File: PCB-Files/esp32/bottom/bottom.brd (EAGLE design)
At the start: 31 x 50 mm, 19 parts, among them X2 ESP32_WROOM32_SKINNY

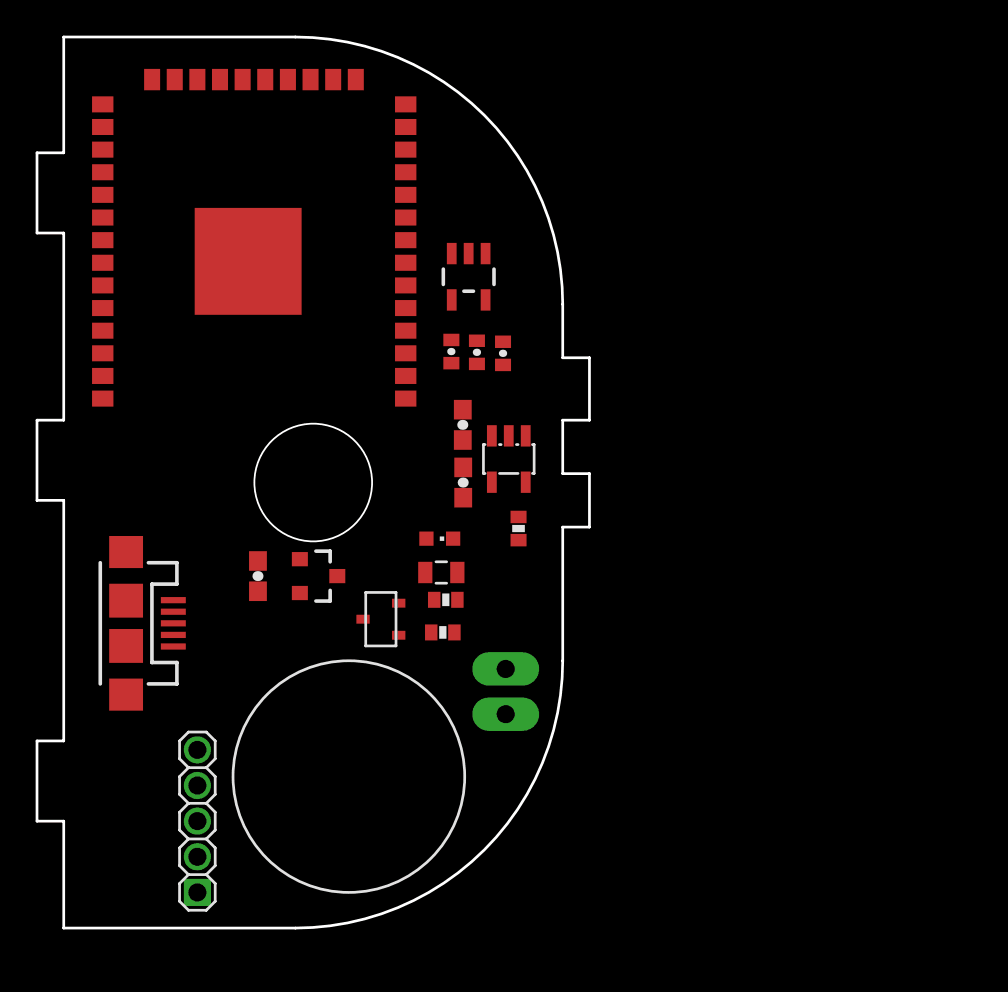
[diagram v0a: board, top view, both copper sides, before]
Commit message: initial files for 4-sided PCBs; no routing done yet
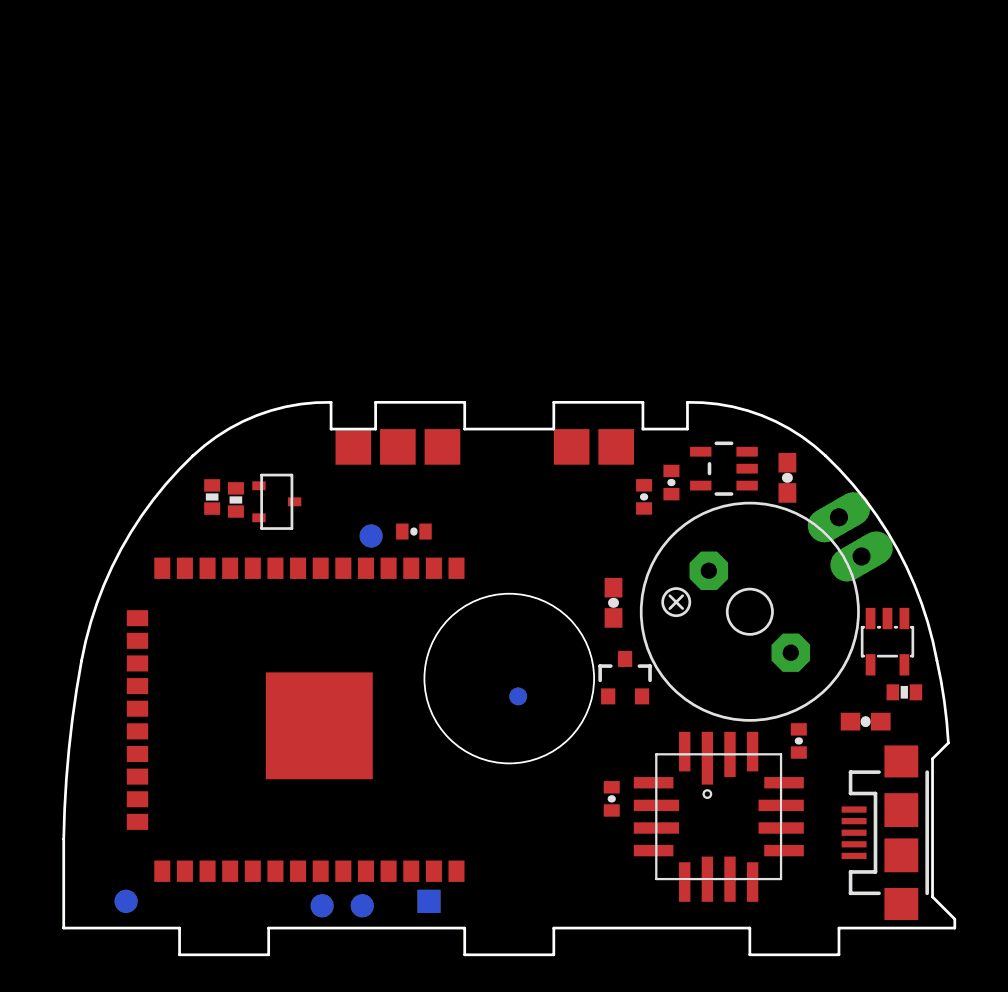
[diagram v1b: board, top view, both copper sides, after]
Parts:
- removed JP3: (no value), pinhead:1_05X2MM
- removed LED1: (no value), adafruit:CHIPLED_0603
- removed R6: 65, SparkFun-Resistors:0805
- added C5, C6: 0.1uF, SparkFun:0402-CAP
- added CAP_MAGNET: TPTP10R, testpad:TP10R
- added GND: TPTP13SQ, testpad:TP13SQ
- added GPIO0, RESET, RX, TX: TPTP13R, testpad:TP13R
- added HALL_1, HALL_2, HALL_3, HALL_GND, HALL_VCC: TPTP20SQ, testpad:TP20SQ
- added SP1: KSS1201, buzzer:KSS1201
- added U$1: ACCELEROMETER_MXR9150MZ, Andy_Sigler_2019:MXR9150MZ
- moved JP1 45.1 mm to (47.0, 5.35), turned to 90 degrees
- moved C1 26.3 mm to (45.0, 11.6), turned to 0 degrees
- moved X2 23.9 mm to (17.0, 11.7), turned to 270 degrees
- moved CHARGER 23.6 mm to (46.2, 16.1)
- moved R22 23.5 mm to (47.2, 13.2), turned to 180 degrees
- moved LIPO 21.7 mm to (43.5, 23.1), turned to 300 degrees
- moved C3 20.0 mm to (30.9, 18.2), turned to 270 degrees
- moved C8 18.5 mm to (40.6, 25.3), turned to 270 degrees
- moved HALL 18.2 mm to (31.5, 14.0), turned to 0 degrees
- moved REG 17.9 mm to (37.0, 25.8), turned to 90 degrees
- moved R10 14.3 mm to (8.33, 24.2), turned to 90 degrees
- moved R15 13.8 mm to (9.66, 24.0), turned to 90 degrees
- moved C10 12.4 mm to (32.6, 24.2), turned to 90 degrees
- moved C4 11.9 mm to (34.1, 25.0), turned to 90 degrees
- moved C2 10.3 mm to (19.6, 22.2), turned to 0 degrees
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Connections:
- removed net A5_IO4: X2.26
- removed net IO12_A11: X2.14
- removed net IO13_A12: X2.16
- removed net IO14_A6: X2.13
- removed net IO15_A8: X2.23
- removed net LED: LED1.A
- removed net N$1: LED1.C, R6.1
- new net ACCEL_SLEEP: U$1.16, U$1.5
- new net ACCEL_X: U$1.13
- new net ACCEL_Y: U$1.12
- new net ACCEL_Z: U$1.2
- new net CAP_SENSE: CAP_MAGNET.TP
- new net D+: JP1.D+
- new net D-: JP1.D-
- new net HALL_1: HALL_1.TP, X2.23
- new net HALL_2: HALL_2.TP, X2.13
- new net HALL_3: HALL_3.TP, X2.16
- net GND: now also C5.2, C6.2, GND.TP, U$1.15, U$1.3, U$1.6, U$1.8; no longer JP3.1, R6.2
- net GPIO0: now also GPIO0.TP; no longer JP3.4
- net HALL_4: now also X2.14
- net HALL_GND: now also HALL_GND.TP
- net HALL_TRANS: now also X2.26
- net RESET: now also RESET.TP; no longer JP3.5
- net RX: now also RX.TP; no longer JP3.2
- net TX: now also TX.TP; no longer JP3.3
- net VCC: now also C5.1, C6.1, HALL_VCC.TP, U$1.11, U$1.14, U$1.4
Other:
- board size 31 x 50 mm -> 50 x 31 mm
- board text added: "To Do: - [S] Order Accel and Hall - [M] Mill PCB to test Accel - [L] Test Accel and Hall with ESP32 - [M] Route PCB traces - [S] Order all parts needed - [L] Mill PCBs - [L] Assemble test PCBs (x2) - [L] Write functional firmware - [M] Final PCB design changes - [S] Order final parts - [L] Mill final PCBs (x6) - [XL] Assemble final PCBs - [L] Add outer shells - [L] Documentation"

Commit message: basic layout; dimension for toothed joints
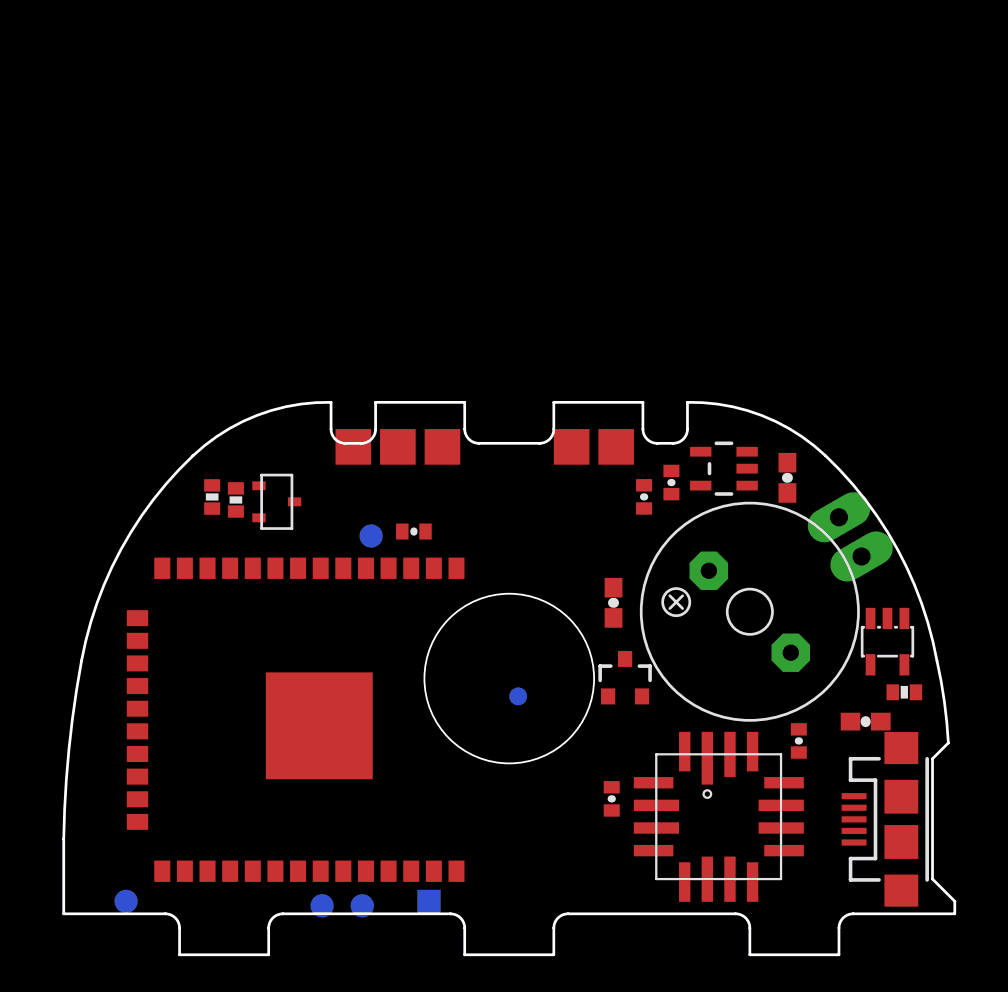
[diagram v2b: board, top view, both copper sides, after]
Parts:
- moved JP1 0.75 mm to (47.0, 6.10)
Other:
- outline, holes or cut-outs redrawn

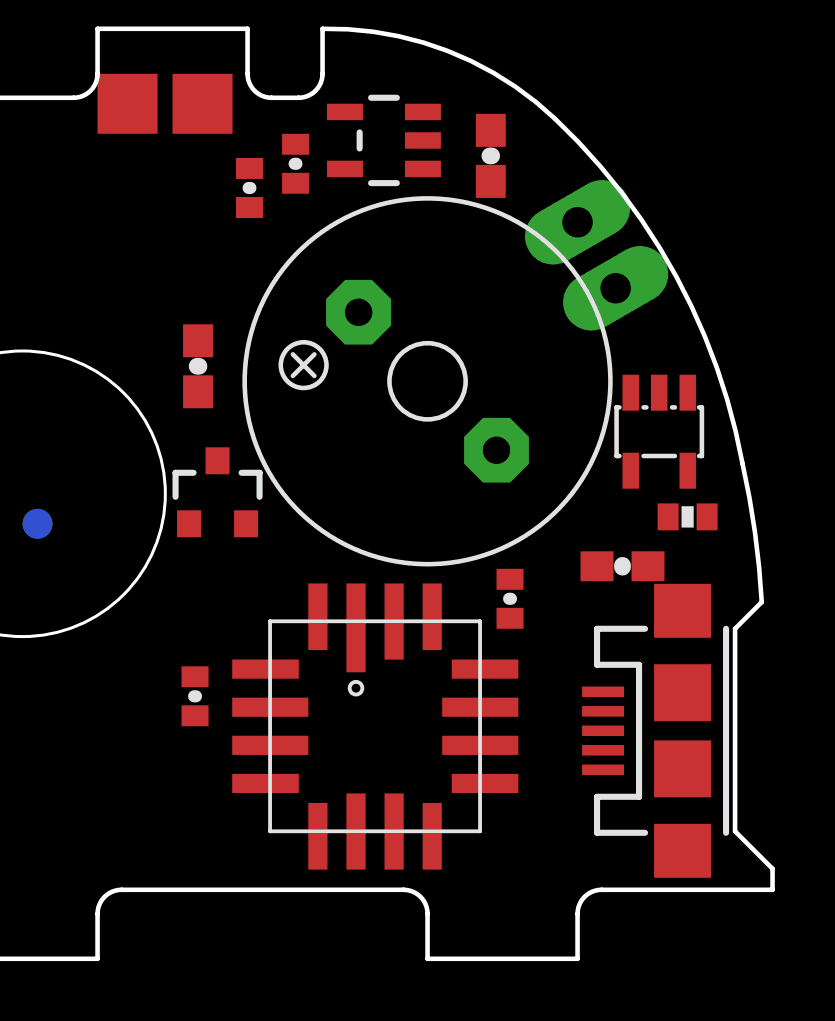
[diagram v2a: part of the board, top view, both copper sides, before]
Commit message: shrink accel pads; accel-test pcb design
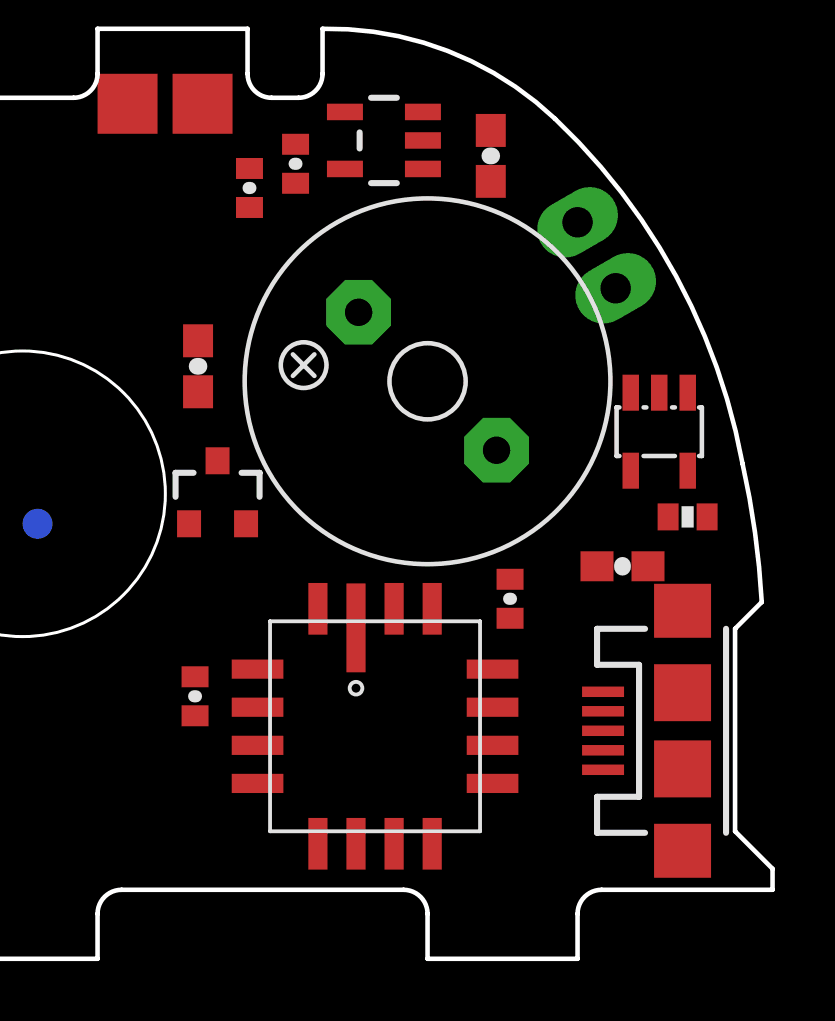
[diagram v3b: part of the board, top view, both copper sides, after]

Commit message: main PCB ready to mill for beta
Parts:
- removed HALL_1, HALL_2, HALL_3, HALL_GND, HALL_VCC: TPTP20SQ, testpad:TP20SQ
- added C7: 0.1uF, SparkFun:0402-CAP
- added C9: 10uF, SparkFun:0402-CAP
- added R1: 10M, SparkFun-Passives:0402-RES
- added TP1, TP10, TP11, TP12, TP2, TP3, TP4, TP5, TP6, TP7, TP8, TP9: TPSQTP10SQ, testpad:TP10SQ
- C10: value 1uF -> 10uF
- C2: value 0.1uF -> 10uf
- C4: value 10uF -> 0.1uF
- HALL: value HALLEFFECT-A1326 -> A1304
- LIPO: device SparkFun:1X02_LONGPADS -> adafruit:JST-PH-2-THM
- R15: value 100k -> 10M
- moved C2 24.4 mm to (44.0, 20.6), turned to 270 degrees
- moved GND 18.8 mm to (1.70, 2.60)
- moved C5 17.9 mm to (42.7, 20.6), turned to 270 degrees
- moved C6 17.7 mm to (32.4, 25.8)
- moved U$1 16.0 mm to (36.8, 22.2), turned to 270 degrees
- moved C4 15.3 mm to (47.4, 17.4), turned to 300 degrees
- moved RESET 14.4 mm to (3.20, 19.1)
- moved C10 13.6 mm to (45.6, 20.4), turned to 210 degrees
- moved REG 11.3 mm to (44.4, 17.2), turned to 300 degrees
- moved R22 11.1 mm to (42.8, 3.03), turned to 270 degrees
- moved SP1 11.1 mm to (36.2, 6.90), turned to 180 degrees
- moved C8 10.9 mm to (42.1, 14.4), turned to 210 degrees
- moved LIPO 9.96 mm to (45.2, 13.2), turned to 210 degrees
- moved CHARGER 7.67 mm to (38.7, 14.4), turned to 90 degrees
- moved CAP_MAGNET 5.16 mm to (29.7, 16.0), flipped to the top
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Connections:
- removed net A13_I35: X2.7
- removed net A1_DAC1: X2.10
- removed net A2_I34: X2.6
- removed net A3_I39: X2.5
- removed net A4_IO36: X2.4
- removed net CAP_SENSE: CAP_MAGNET.TP
- removed net IO32_A7: X2.8
- removed net IO33_A9: X2.9
- removed net SCK: X2.29
- removed net SDA: X2.37
- new net IO13_A12: X2.16
- new net IO14_A6: X2.13
- new net IO15_A8: X2.23
- new net SPEAKER: SP1.+, X2.37
- new net TOUCH: CAP_MAGNET.TP, TP11.TP, TP12.TP, X2.26
- net ACCEL_SLEEP: now also R1.1, X2.29
- net ACCEL_X: now also X2.4
- net ACCEL_Y: now also X2.5
- net ACCEL_Z: now also X2.6
- net GND: now also C7.2, C9.2, LIPO.2, SP1.-; no longer LIPO.1
- net HALL_1: now also TP10.TP, TP3.TP, X2.7; no longer HALL_1.TP, X2.23
- net HALL_2: now also TP4.TP, TP9.TP, X2.8; no longer HALL_2.TP, X2.13
- net HALL_3: now also TP5.TP, TP8.TP, X2.9; no longer HALL_3.TP, X2.16
- net HALL_4: now also X2.10; no longer X2.14
- net HALL_GND: now also TP6.TP, TP7.TP; no longer HALL_GND.TP
- net HALL_TRANS: now also X2.14; no longer X2.26
- net VBATT: now also LIPO.1; no longer LIPO.2
- net VCC: now also C7.1, C9.1, R1.2, TP1.TP, TP2.TP; no longer HALL_VCC.TP
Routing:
- net VCC: track 0.00 -> 77.2 mm, vias 0 -> 2
- net ACCEL_SLEEP: track 0.00 -> 73.6 mm, vias 0 -> 3
- net HALL_GND: track 0.00 -> 72.6 mm, vias 0 -> 2
- net HALL_4: track 0.00 -> 45.1 mm, vias 0 -> 2
- net TOUCH: track 0.00 -> 40.4 mm
- net ACCEL_Z: track 0.00 -> 32.5 mm, vias 0 -> 2
- net HALL_1: track 0.00 -> 24.5 mm, vias 0 -> 2
- net HALL_2: track 0.00 -> 21.6 mm
- net ACCEL_Y: track 0.00 -> 19.4 mm
- net RESET: track 0.00 -> 19.4 mm, vias 0 -> 1
- net ACCEL_X: track 0.00 -> 17.9 mm
- net SPEAKER: track 0.00 -> 17.6 mm, vias 0 -> 1
- net 5V: track 0.00 -> 16.1 mm
- net HALL_3: track 0.00 -> 15.3 mm
- net N$2: track 0.00 -> 12.2 mm
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- added copper zone on layer 1, net GND
- added copper zone on layer 16, net GND
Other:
- board text removed: "To Do: - [S] Order Accel and Hall - [M] Mill PCB to test Accel - [L] Test Accel and Hall with ESP32 - [M] Route PCB traces - [S] Order all parts needed - [L] Mill PCBs - [L] Assemble test PCBs (x2) - [L] Write functional firmware - [M] Final PCB design changes - [S] Order final parts - [L] Mill final PCBs (x6) - [XL] Assemble final PCBs - [L] Add outer shells - [L] Documentation"
